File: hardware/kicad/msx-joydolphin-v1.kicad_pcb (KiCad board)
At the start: 2 copper layers, 56 x 32 mm, 14 parts, among them J1 J1 MSX, J2 J2 GCN, J3 DEBUG, Q1 BSS138

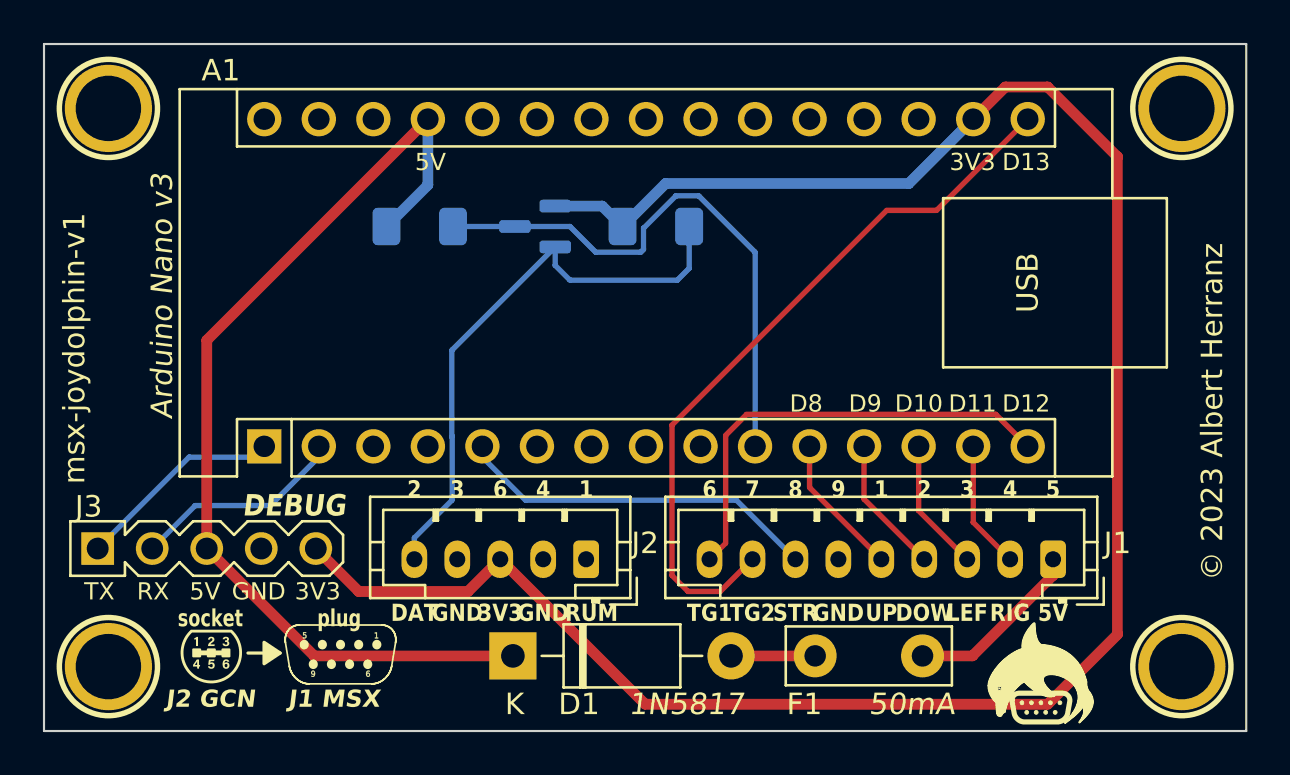
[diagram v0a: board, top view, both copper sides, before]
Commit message: hardware: miscelanoues enhancements
- Add top copper fill area for ground
  Save some chemicals when etching the top layer, and possibly enhance signal
  integrity.
- Change board width
  Reduce board width from 56mm to 55mm to allow using alterante off-the-shelf
  plastic case.
- Label all soldered pads on bottom side
  Add silkscreen labels to all pads requiring soldering on the bottom side
  of the board.

Signed-off-by: Albert Herranz <albert_herranz@yahoo.es>
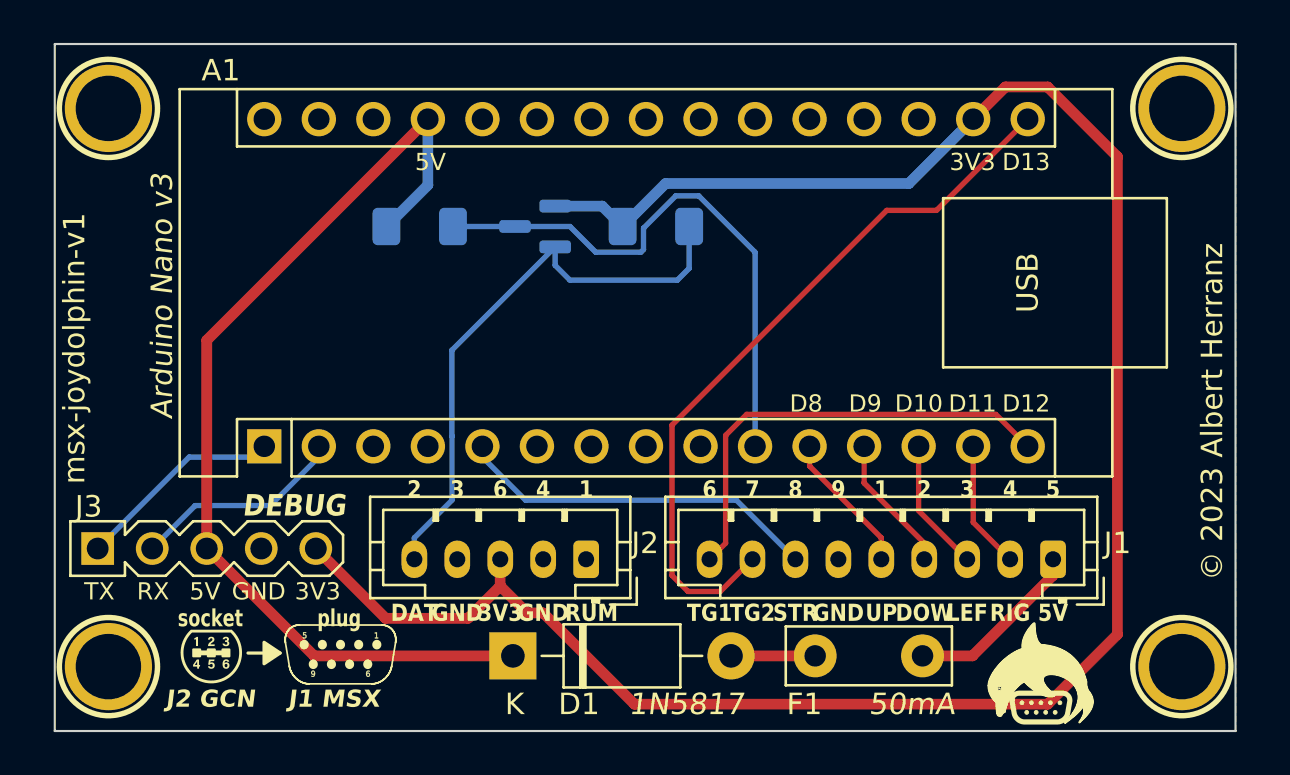
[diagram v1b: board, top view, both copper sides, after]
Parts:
- moved REF** 1.68 mm to (92.8, 56.8)
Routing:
- net /VCC_3V3: track 95.8 -> 97.1 mm
- added copper zone on F.Cu, net GND
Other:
- board size 56 x 32 mm -> 55 x 32 mm
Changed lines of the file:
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@@
   )
   (footprint "Symbol:OSHW-Logo_7.5x8mm_SilkScreen" (layer "B.Cu")
-    (at 93.5 58.25 180)
+    (at 92.75 56.75 180)
     (descr "Open Source Hardware Logo")
     (tags "Logo OSHW")
@@
   (gr_line (start 57.781493 63.863657) (end 57.761804 63.833728)
     (stroke (width 0.079472) (type solid)) (layer "F.SilkS"))
-  (gr_rect (start 41.5 36.5) (end 97.5 68.5)
+  (gr_rect (start 42 36.5) (end 97 68.5)
     (stroke (width 0.1) (type default)) (fill none) (layer "Edge.Cuts"))
   (gr_text "STR" (at 76.5 62.5) (layer "B.SilkS")
@@
     (effects (font (size 0.8 0.8) (thickness 0.2)) (justify top mirror))
   )
+  (gr_text "D13" (at 87.25 42) (layer "B.SilkS")
+    (effects (font (size 0.8 0.8) (thickness 0.2)) (justify mirror))
+  )
   (gr_text "5V" (at 59.5 42) (layer "B.SilkS")
     (effects (font (size 0.8 0.8) (thickness 0.2)) (justify mirror))
   )
+  (gr_text "GND" (at 59.5 53.25) (layer "B.SilkS")
+    (effects (font (size 0.8 0.8) (thickness 0.2)) (justify mirror))
+  )
   (gr_text "TX" (at 51.75 53.25) (layer "B.SilkS")
     (effects (font (size 0.8 0.8) (thickness 0.2)) (justify mirror))
@@
     (effects (font (size 0.8 0.8) (thickness 0.2)) (justify mirror))
   )
+  (gr_text "D11" (at 84.75 53.25) (layer "B.SilkS")
+    (effects (font (size 0.8 0.8) (thickness 0.2)) (justify mirror))
+  )
   (gr_text "DAT\n5V\nD7" (at 74.75 52.25) (layer "B.SilkS")
     (effects (font (size 0.8 0.8) (thickness 0.2)) (justify mirror))
@@
     (effects (font (size 0.8 0.8) (thickness 0.2)) (justify mirror))
   )
+  (gr_text "D12" (at 87.25 53.25) (layer "B.SilkS")
+    (effects (font (size 0.8 0.8) (thickness 0.2)) (justify mirror))
+  )
+  (gr_text "D9" (at 79.75 53.25) (layer "B.SilkS")
+    (effects (font (size 0.8 0.8) (thickness 0.2)) (justify mirror))
+  )
+  (gr_text "D10" (at 82.25 53.25) (layer "B.SilkS")
+    (effects (font (size 0.8 0.8) (thickness 0.2)) (justify mirror))
+  )
   (gr_text "3V3" (at 54.25 62) (layer "B.SilkS")
     (effects (font (size 0.8 0.8) (thickness 0.2)) (justify mirror))
@@
     (effects (font (size 0.8 0.8) (thickness 0.2)) (justify mirror))
   )
+  (gr_text "D8" (at 77 53.25) (layer "B.SilkS")
+    (effects (font (size 0.8 0.8) (thickness 0.2)) (justify mirror))
+  )
+  (gr_text "GND" (at 54.25 42) (layer "B.SilkS")
+    (effects (font (size 0.8 0.8) (thickness 0.2)) (justify mirror))
+  )
   (gr_text "RIG" (at 86.5 63) (layer "F.SilkS")
     (effects (font (size 0.8 0.7) (thickness 0.15) bold))
@@
     (stroke (width 0.15) (type dot))  )
   (dimension (type orthogonal) (layer "Cmts.User")
-    (pts (xy 41.5 37.5) (xy 97.5 37))
+    (pts (xy 42 37.5) (xy 97 37))
     (height -2)
     (orientation 0)
-    (gr_text "56.0000 mm" (at 69.5 34.35) (layer "Cmts.User")
+    (gr_text "55.0000 mm" (at 69.5 34.35) (layer "Cmts.User")
       (effects (font (size 1 1) (thickness 0.15)))
     )
@@
   (segment (start 70.925 43.575) (end 69.425 45.075) (width 0.25) (layer "B.Cu") (net 10))
   (segment (start 74.62 46.195) (end 72 43.575) (width 0.25) (layer "B.Cu") (net 10))
-  (segment (start 77.16 55.24) (end 77.16 57.16) (width 0.25) (layer "F.Cu") (net 11))
-  (segment (start 77.16 57.16) (end 80.5 60.5) (width 0.25) (layer "F.Cu") (net 11))
-  (segment (start 79.7 55.24) (end 79.7 57.7) (width 0.25) (layer "F.Cu") (net 12))
-  (segment (start 79.7 57.7) (end 82.5 60.5) (width 0.25) (layer "F.Cu") (net 12))
+  (segment (start 77.16 56.16) (end 80.5 59.5) (width 0.25) (layer "F.Cu") (net 11))
+  (segment (start 80.5 59.5) (end 80.5 60.5) (width 0.25) (layer "F.Cu") (net 11))
+  (segment (start 77.16 55.24) (end 77.16 56.16) (width 0.25) (layer "F.Cu") (net 11))
+  (segment (start 82.5 59.75) (end 82.5 60.5) (width 0.25) (layer "F.Cu") (net 12))
+  (segment (start 79.7 56.95) (end 82.5 59.75) (width 0.25) (layer "F.Cu") (net 12))
+  (segment (start 79.7 55.24) (end 79.7 56.95) (width 0.25) (layer "F.Cu") (net 12))
   (segment (start 82.24 58.24) (end 84.5 60.5) (width 0.25) (layer "F.Cu") (net 13))
   (segment (start 82.24 55.24) (end 82.24 58.24) (width 0.25) (layer "F.Cu") (net 13))
@@
   (segment (start 74.38 60) (end 74.38 59.87) (width 0.25) (layer "F.Cu") (net 16))
   (segment (start 83.07 44.25) (end 80.75 44.25) (width 0.25) (layer "F.Cu") (net 16))
-  (segment (start 69.5 67.25) (end 62.75 60.5) (width 0.5) (layer "F.Cu") (net 17))
+  (segment (start 86.28 38.5) (end 88.25 38.5) (width 0.5) (layer "F.Cu") (net 17))
+  (segment (start 88.25 38.5) (end 91.5 41.75) (width 0.5) (layer "F.Cu") (net 17))
+  (segment (start 62.75 61.75) (end 61.25 63.25) (width 0.5) (layer "F.Cu") (net 17))
+  (segment (start 64 63) (end 62.75 61.75) (width 0.5) (layer "F.Cu") (net 17))
+  (segment (start 69 67.25) (end 64.75 63) (width 0.5) (layer "F.Cu") (net 17))
   (segment (start 84.78 40) (end 86.28 38.5) (width 0.5) (layer "F.Cu") (net 17))
-  (segment (start 88.25 67.25) (end 69.5 67.25) (width 0.5) (layer "F.Cu") (net 17))
-  (segment (start 61.25 62) (end 56.16 62) (width 0.5) (layer "F.Cu") (net 17))
+  (segment (start 88.25 67.25) (end 69 67.25) (width 0.5) (layer "F.Cu") (net 17))
+  (segment (start 64.75 63) (end 64 63) (width 0.5) (layer "F.Cu") (net 17))
   (segment (start 91.5 64) (end 88.25 67.25) (width 0.5) (layer "F.Cu") (net 17))
-  (segment (start 86.28 38.5) (end 88.25 38.5) (width 0.5) (layer "F.Cu") (net 17))
+  (segment (start 57.41 63.25) (end 54.16 60) (width 0.5) (layer "F.Cu") (net 17))
   (segment (start 91.5 41.75) (end 91.5 64) (width 0.5) (layer "F.Cu") (net 17))
-  (segment (start 88.25 38.5) (end 91.5 41.75) (width 0.5) (layer "F.Cu") (net 17))
-  (segment (start 56.16 62) (end 54.16 60) (width 0.5) (layer "F.Cu") (net 17))
-  (segment (start 62.75 60.5) (end 61.25 62) (width 0.5) (layer "F.Cu") (net 17))
+  (segment (start 62.75 60.5) (end 62.75 61.75) (width 0.5) (layer "F.Cu") (net 17))
+  (segment (start 61.25 63.25) (end 57.41 63.25) (width 0.5) (layer "F.Cu") (net 17))
   (segment (start 65.31 44.05) (end 67.5 44.05) (width 0.5) (layer "B.Cu") (net 17))
   (segment (start 81.78 43) (end 70.45 43) (width 0.5) (layer "B.Cu") (net 17))
@@
   (segment (start 60.505 54.774009) (end 60.5 54.769009) (width 0.25) (layer "B.Cu") (net 32))
   (segment (start 65.31 45.95) (end 65.31 46.81) (width 0.25) (layer "B.Cu") (net 32))
-  (zone locked (net 4) (net_name "GND") (layer "B.Cu") (hatch edge 0.5)
+  (zone (net 4) (net_name "GND") (layer "F.Cu") (hatch edge 0.5)
+    (priority 1)
+    (connect_pads (clearance 0.5))
+    (min_thickness 0.25) (filled_areas_thickness no)
+    (fill yes (thermal_gap 0.5) (thermal_bridge_width 0.5))
+    (polygon
+      (pts
+        (xy 42 36.5)
+        (xy 97 36.5)
+        (xy 97 68.5)
+        (xy 42 68.5)
+      )
+    )
+  )
+  (zone (net 4) (net_name "GND") (layer "B.Cu") (hatch edge 0.5)
     (connect_pads (clearance 0.5))
     (min_thickness 0.25) (filled_areas_thickness no)
@@
     (polygon
       (pts
-        (xy 41.5 36.5)
-        (xy 97.5 36.5)
-        (xy 97.5 68.5)
-        (xy 41.5 68.5)
+        (xy 42 36.5)
+        (xy 97 36.5)
+        (xy 97 68.5)
+        (xy 42 68.5)
       )
     )

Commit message: board: use OUT,TRGA,TRGB instead of STR,TRG1,TRG2
Signed-off-by: Albert Herranz <albert_herranz@yahoo.es>
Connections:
- net /MSX_STROBE renamed /MSX_OUT
- net /MSX_TRIG1 renamed /MSX_TRIGA
- net /MSX_TRIG2 renamed /MSX_TRIGB
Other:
- board text added: "Build 1b"
- board text added: "COM"
- board text added: "TGA"
- board text added: "TGB"
- board text removed: "TG1"
- board text removed: "TG2"
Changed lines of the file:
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@@
   (title_block
     (title "msx-joydolphin: A Gamecube controller adapter for MSX")
-    (date "2023-09-23")
-    (rev "v1")
+    (date "2024-02-21")
+    (rev "v1 Build1b")
     (company "Albert Herranz")
   )
@@
   (net 3 "unconnected-(A1-~{RESET}-Pad3)")
   (net 4 "GND")
-  (net 5 "/MSX_STROBE")
+  (net 5 "/MSX_OUT")
   (net 6 "unconnected-(A1-D3-Pad6)")
   (net 7 "unconnected-(A1-D4-Pad7)")
@@
   (net 13 "/MSX_LEFT")
   (net 14 "/MSX_RIGHT")
-  (net 15 "/MSX_TRIG1")
-  (net 16 "/MSX_TRIG2")
+  (net 15 "/MSX_TRIGA")
+  (net 16 "/MSX_TRIGB")
   (net 17 "/VCC_3V3")
   (net 18 "unconnected-(A1-AREF-Pad18)")
@@
       (net 4 "GND") (pinfunction "GND") (pintype "power_in"))
     (pad "5" thru_hole oval (at 0 10.16 90) (size 1.6 1.6) (drill 1) (layers "*.Cu" "*.Mask")
-      (net 5 "/MSX_STROBE") (pinfunction "D2") (pintype "bidirectional"))
+      (net 5 "/MSX_OUT") (pinfunction "D2") (pintype "bidirectional"))
     (pad "6" thru_hole oval (at 0 12.7 90) (size 1.6 1.6) (drill 1) (layers "*.Cu" "*.Mask")
       (net 6 "unconnected-(A1-D3-Pad6)") (pinfunction "D3") (pintype "bidirectional+no_connect"))
@@
       (net 14 "/MSX_RIGHT") (pinfunction "D11") (pintype "bidirectional"))
     (pad "15" thru_hole oval (at 0 35.56 90) (size 1.6 1.6) (drill 1) (layers "*.Cu" "*.Mask")
-      (net 15 "/MSX_TRIG1") (pinfunction "D12") (pintype "bidirectional"))
+      (net 15 "/MSX_TRIGA") (pinfunction "D12") (pintype "bidirectional"))
     (pad "16" thru_hole oval (at 15.24 35.56 90) (size 1.6 1.6) (drill 1) (layers "*.Cu" "*.Mask")
-      (net 16 "/MSX_TRIG2") (pinfunction "D13") (pintype "bidirectional"))
+      (net 16 "/MSX_TRIGB") (pinfunction "D13") (pintype "bidirectional"))
     (pad "17" thru_hole oval (at 15.24 33.02 90) (size 1.6 1.6) (drill 1) (layers "*.Cu" "*.Mask")
       (net 17 "/VCC_3V3") (pinfunction "3V3") (pintype "power_out"))
@@
       (net 4 "GND") (pinfunction "6") (pintype "passive"))
     (pad "7" thru_hole oval (at 12 0 180) (size 1.2 1.75) (drill 0.75) (layers "*.Cu" "*.Mask")
-      (net 5 "/MSX_STROBE") (pinfunction "7") (pintype "passive"))
+      (net 5 "/MSX_OUT") (pinfunction "7") (pintype "passive"))
     (pad "8" thru_hole oval (at 14 0 180) (size 1.2 1.75) (drill 0.75) (layers "*.Cu" "*.Mask")
-      (net 16 "/MSX_TRIG2") (pinfunction "8") (pintype "passive"))
+      (net 16 "/MSX_TRIGB") (pinfunction "8") (pintype "passive"))
     (pad "9" thru_hole oval (at 16 0 180) (size 1.2 1.75) (drill 0.75) (layers "*.Cu" "*.Mask")
-      (net 15 "/MSX_TRIG1") (pinfunction "9") (pintype "passive"))
+      (net 15 "/MSX_TRIGA") (pinfunction "9") (pintype "passive"))
     (model "${KICAD6_3DMODEL_DIR}/Connector_JST.3dshapes/JST_PH_B9B-PH-K_1x09_P2.00mm_Vertical.wrl"
       (offset (xyz 0 0 0))
@@
     (descr "Open Source Hardware Logo")
     (tags "Logo OSHW")
-    (attr board_only exclude_from_pos_files exclude_from_bom allow_missing_courtyard)
+    (attr exclude_from_pos_files exclude_from_bom)
     (fp_text reference "REF**" (at 0 0) (layer "F.SilkS") hide
-        (effects (font (size 1 1) (thickness 0.15)))
+        (effects (font (size 1 1) (thickness 0.15)) (justify mirror))
     )
     (fp_text value "OSHW-Logo_7.5x8mm_SilkScreen" (at 0.75 0) (layer "B.Fab") hide
@@
     (effects (font (size 0.8 0.7) (thickness 0.15) bold))
   )
+  (gr_text "Build 1b" (at 45.2 57 90) (layer "F.SilkS")
+    (effects (font (size 1 1) (thickness 0.2)) (justify left bottom))
+  )
   (gr_text "DOW" (at 82.5 63) (layer "F.SilkS")
     (effects (font (size 0.8 0.7) (thickness 0.15) bold))
@@
     (effects (font (size 0.8 0.6) (thickness 0.1) bold))
   )
-  (gr_text "TG1" (at 72.5 63) (layer "F.SilkS")
+  (gr_text "TGA" (at 72.5 63) (layer "F.SilkS")
     (effects (font (size 0.8 0.7) (thickness 0.15) bold))
   )
@@
     (effects (font (size 0.8 0.7) (thickness 0.15) bold))
   )
-  (gr_text "STR" (at 76.5 63) (layer "F.SilkS")
+  (gr_text "COM" (at 76.5 63) (layer "F.SilkS")
     (effects (font (size 0.8 0.7) (thickness 0.15) bold))
   )
@@
     (effects (font (size 1 1) (thickness 0.2)) (justify left bottom))
   )
-  (gr_text "TG2" (at 74.5 63) (layer "F.SilkS")
+  (gr_text "TGB" (at 74.5 63) (layer "F.SilkS")
     (effects (font (size 0.8 0.7) (thickness 0.15) bold))
   )
